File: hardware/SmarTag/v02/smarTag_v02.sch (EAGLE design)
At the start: 21 parts, among them U1 ADXL362

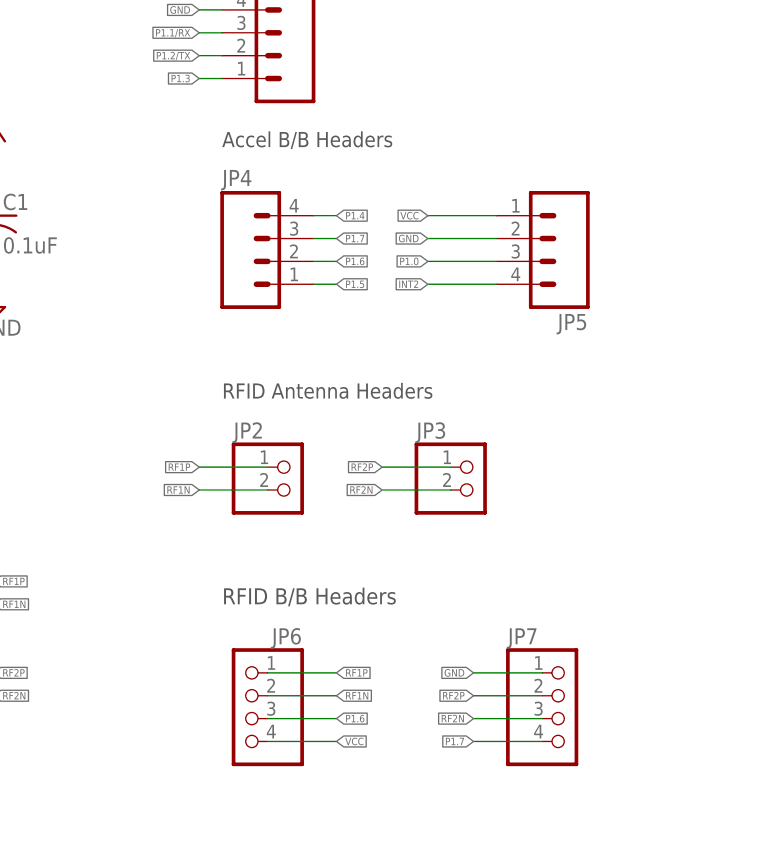
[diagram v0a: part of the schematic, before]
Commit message: hw: Remove JP4-7 from schematic. Add basic board.
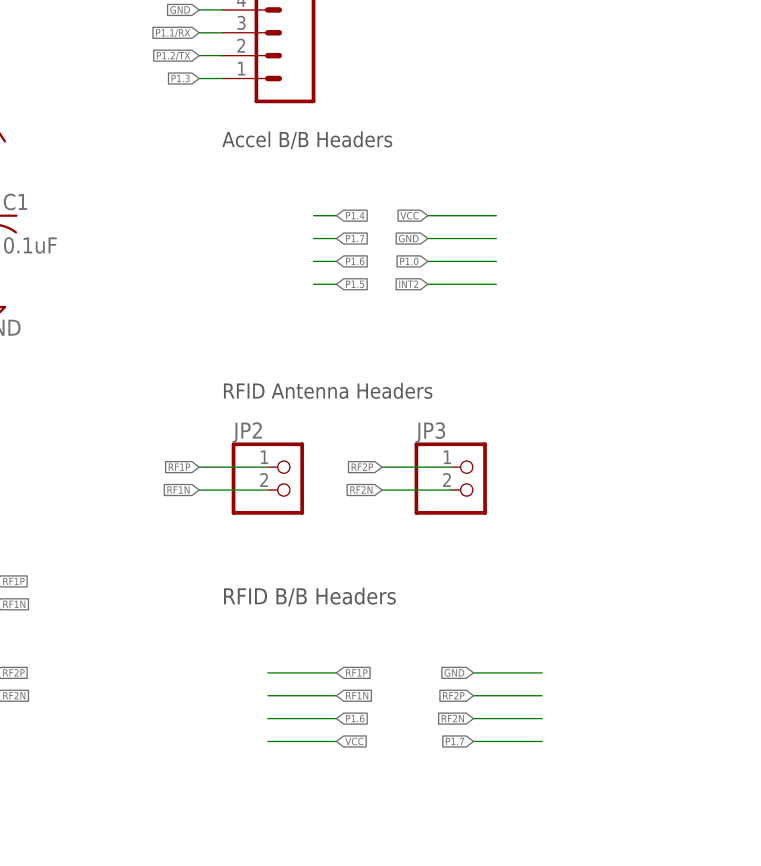
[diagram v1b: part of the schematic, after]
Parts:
- removed JP4, JP5: (no value), SparkFun-Connectors:M04LOCK
- removed JP6, JP7: (no value), pinhead:PINHD-1X4
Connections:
- net GND: no longer JP5.2, JP7.1
- net INT2: no longer JP5.4
- net P1.0: no longer JP5.3
- net P1.4: no longer JP4.4
- net P1.5: no longer JP4.1
- net P1.6: no longer JP4.2, JP6.3
- net P1.7: no longer JP4.3, JP7.4
- net RF1N: no longer JP6.2
- net RF1P: no longer JP6.1
- net RF2N: no longer JP7.3
- net RF2P: no longer JP7.2
- net VCC: no longer JP5.1, JP6.4
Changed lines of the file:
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@@
 <part name="P+4" library="supply1" deviceset="VCC" device=""/>
 <part name="SUPPLY1" library="supply2" deviceset="GND" device=""/>
-<part name="JP6" library="pinhead" deviceset="PINHD-1X4" device=""/>
-<part name="JP7" library="pinhead" deviceset="PINHD-1X4" device=""/>
 <part name="LED1" library="led" deviceset="LED" device="CHIP-LED0805"/>
 <part name="R3" library="rcl" deviceset="R-US_" device="R0805" value="470"/>
@@
 <part name="JP9" library="SparkFun-Connectors" deviceset="M05" device="LOCK"/>
 <part name="JP8" library="SparkFun-Connectors" deviceset="M03" device="LOCK"/>
-<part name="JP4" library="SparkFun-Connectors" deviceset="M04" device="LOCK"/>
 <part name="S1" library="switch-omron" deviceset="10-XX" device=""/>
-<part name="JP5" library="SparkFun-Connectors" deviceset="M04" device="LOCK"/>
 </parts>
 <sheets>
@@
 <instance part="P+4" gate="VCC" x="139.7" y="162.56" rot="R270"/>
 <instance part="SUPPLY1" gate="GND" x="119.38" y="160.02"/>
-<instance part="JP6" gate="A" x="119.38" y="30.48" rot="MR0"/>
-<instance part="JP7" gate="A" x="154.94" y="30.48"/>
 <instance part="LED1" gate="G$1" x="132.08" y="180.34" rot="R90"/>
 <instance part="R3" gate="G$1" x="119.38" y="180.34"/>
@@
 <instance part="JP9" gate="G$1" x="124.46" y="106.68" rot="MR0"/>
 <instance part="JP8" gate="G$1" x="160.02" y="134.62" rot="MR0"/>
-<instance part="JP4" gate="G$1" x="121.92" y="81.28"/>
 <instance part="S1" gate="1" x="162.56" y="180.34" rot="R270"/>
-<instance part="JP5" gate="G$1" x="152.4" y="83.82" rot="R180"/>
 </instances>
 <busses>
@@
 <wire x1="147.32" y1="86.36" x2="139.7" y2="86.36" width="0.1524" layer="91"/>
 <label x="139.7" y="86.36" size="0.8128" layer="91" rot="MR0" xref="yes"/>
-<pinref part="JP5" gate="G$1" pin="1"/>
 </segment>
 <segment>
@@
 </segment>
 <segment>
-<pinref part="JP6" gate="A" pin="4"/>
 <wire x1="121.92" y1="27.94" x2="129.54" y2="27.94" width="0.1524" layer="91"/>
 <label x="129.54" y="27.94" size="0.8128" layer="91" xref="yes"/>
@@
 <wire x1="147.32" y1="81.28" x2="139.7" y2="81.28" width="0.1524" layer="91"/>
 <label x="139.7" y="81.28" size="0.8128" layer="91" rot="MR0" xref="yes"/>
-<pinref part="JP5" gate="G$1" pin="3"/>
 </segment>
 </net>
@@
 <wire x1="127" y1="86.36" x2="129.54" y2="86.36" width="0.1524" layer="91"/>
 <label x="129.54" y="86.36" size="0.8128" layer="91" rot="MR180" xref="yes"/>
-<pinref part="JP4" gate="G$1" pin="4"/>
 </segment>
 </net>
@@
 <wire x1="129.54" y1="78.74" x2="127" y2="78.74" width="0.1524" layer="91"/>
 <label x="129.54" y="78.74" size="0.8128" layer="91" xref="yes"/>
-<pinref part="JP4" gate="G$1" pin="1"/>
 </segment>
 </net>
@@
 <wire x1="129.54" y1="83.82" x2="127" y2="83.82" width="0.1524" layer="91"/>
 <label x="129.54" y="83.82" size="0.8128" layer="91" rot="MR180" xref="yes"/>
-<pinref part="JP4" gate="G$1" pin="3"/>
-</segment>
-<segment>
-<pinref part="JP7" gate="A" pin="4"/>
+</segment>
+<segment>
 <wire x1="152.4" y1="27.94" x2="144.78" y2="27.94" width="0.1524" layer="91"/>
 <label x="144.78" y="27.94" size="0.8128" layer="91" rot="MR0" xref="yes"/>
@@
 <wire x1="127" y1="81.28" x2="129.54" y2="81.28" width="0.1524" layer="91"/>
 <label x="129.54" y="81.28" size="0.8128" layer="91" rot="MR180" xref="yes"/>
-<pinref part="JP4" gate="G$1" pin="2"/>
-</segment>
-<segment>
-<pinref part="JP6" gate="A" pin="3"/>
+</segment>
+<segment>
 <wire x1="121.92" y1="30.48" x2="129.54" y2="30.48" width="0.1524" layer="91"/>
 <label x="129.54" y="30.48" size="0.8128" layer="91" xref="yes"/>
@@
 <wire x1="139.7" y1="83.82" x2="147.32" y2="83.82" width="0.1524" layer="91"/>
 <label x="139.7" y="83.82" size="0.8128" layer="91" rot="MR0" xref="yes"/>
-<pinref part="JP5" gate="G$1" pin="2"/>
 </segment>
 <segment>
@@
 </segment>
 <segment>
-<pinref part="JP7" gate="A" pin="1"/>
 <wire x1="152.4" y1="35.56" x2="144.78" y2="35.56" width="0.1524" layer="91"/>
 <label x="144.78" y="35.56" size="0.8128" layer="91" rot="MR0" xref="yes"/>
@@
 </segment>
 <segment>
-<pinref part="JP6" gate="A" pin="1"/>
 <wire x1="121.92" y1="35.56" x2="129.54" y2="35.56" width="0.1524" layer="91"/>
 <label x="129.54" y="35.56" size="0.8128" layer="91" xref="yes"/>
@@
 </segment>
 <segment>
-<pinref part="JP6" gate="A" pin="2"/>
 <wire x1="129.54" y1="33.02" x2="121.92" y2="33.02" width="0.1524" layer="91"/>
 <label x="129.54" y="33.02" size="0.8128" layer="91" xref="yes"/>
@@
 </segment>
 <segment>
-<pinref part="JP7" gate="A" pin="3"/>
 <wire x1="152.4" y1="30.48" x2="144.78" y2="30.48" width="0.1524" layer="91"/>
 <label x="144.78" y="30.48" size="0.8128" layer="91" rot="MR0" xref="yes"/>
@@
 </segment>
 <segment>
-<pinref part="JP7" gate="A" pin="2"/>
 <wire x1="152.4" y1="33.02" x2="144.78" y2="33.02" width="0.1524" layer="91"/>
 <label x="144.78" y="33.02" size="0.8128" layer="91" rot="MR0" xref="yes"/>
@@
 <wire x1="139.7" y1="78.74" x2="147.32" y2="78.74" width="0.1524" layer="91"/>
 <label x="139.7" y="78.74" size="0.8128" layer="91" rot="MR0" xref="yes"/>
-<pinref part="JP5" gate="G$1" pin="4"/>
-</segment>
-<segment>
+</segment>
+<segment>

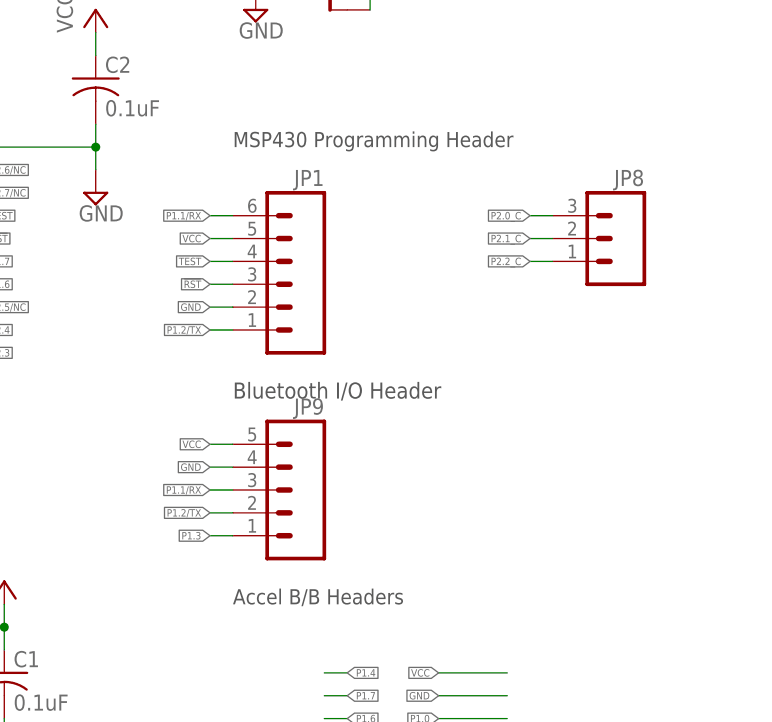
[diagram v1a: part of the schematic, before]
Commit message: hw: Renumber JP headers and fix BT header.
Remove P1.3 signal from BT daughter board header.
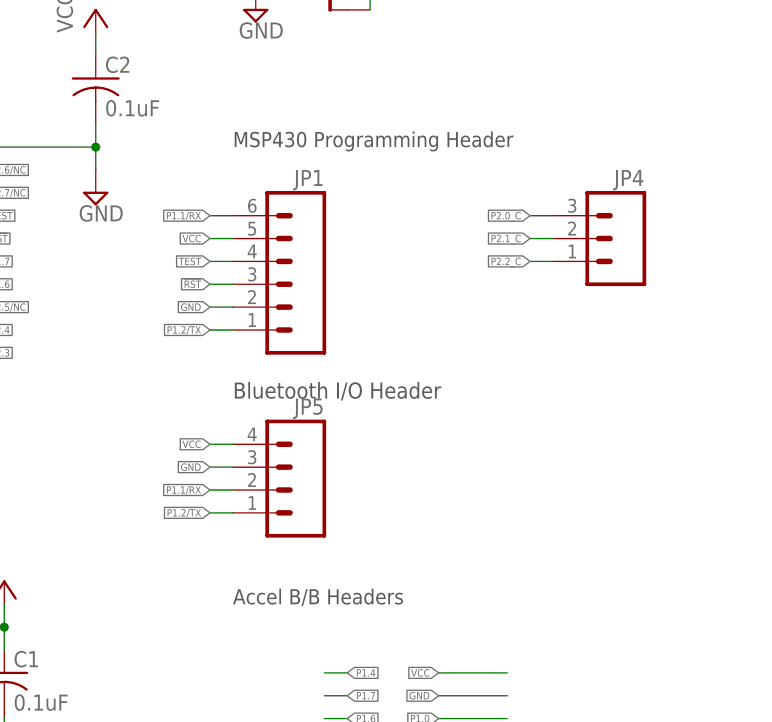
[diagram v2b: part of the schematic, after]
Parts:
- removed JP9: (no value), SparkFun-Connectors:M05LOCK
- added JP5: (no value), SparkFun-Connectors:M04LOCK
- renumbered JP8 to JP4
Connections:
- net GND: now also JP5.3; no longer JP9.4
- net P1.1/RX: now also JP5.2; no longer JP9.3
- net P1.2/TX: now also JP5.1; no longer JP9.2
- net P1.3: no longer JP9.1
- net VCC: now also JP5.4; no longer JP9.5
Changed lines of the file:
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@@
 <part name="SUPPLY5" library="supply2" deviceset="GND" device=""/>
 <part name="JP1" library="SparkFun-Connectors" deviceset="M06" device="LOCK"/>
-<part name="JP9" library="SparkFun-Connectors" deviceset="M05" device="LOCK"/>
-<part name="JP8" library="SparkFun-Connectors" deviceset="M03" device="LOCK"/>
+<part name="JP4" library="SparkFun-Connectors" deviceset="M03" device="LOCK"/>
 <part name="S1" library="switch-omron" deviceset="10-XX" device=""/>
+<part name="JP5" library="SparkFun-Connectors" deviceset="M04" device="LOCK"/>
 </parts>
 <sheets>
@@
 <instance part="SUPPLY5" gate="GND" x="142.24" y="177.8"/>
 <instance part="JP1" gate="G$1" x="121.92" y="129.54" rot="MR0"/>
-<instance part="JP9" gate="G$1" x="124.46" y="106.68" rot="MR0"/>
-<instance part="JP8" gate="G$1" x="160.02" y="134.62" rot="MR0"/>
+<instance part="JP4" gate="G$1" x="160.02" y="134.62" rot="MR0"/>
 <instance part="S1" gate="1" x="162.56" y="180.34" rot="R270"/>
+<instance part="JP5" gate="G$1" x="121.92" y="106.68" rot="MR0"/>
 </instances>
 <busses>
@@
 <wire x1="116.84" y1="111.76" x2="114.3" y2="111.76" width="0.1524" layer="91"/>
 <label x="114.3" y="111.76" size="0.8128" layer="91" rot="MR0" xref="yes"/>
-<pinref part="JP9" gate="G$1" pin="5"/>
+<pinref part="JP5" gate="G$1" pin="4"/>
 </segment>
 </net>
@@
 <wire x1="116.84" y1="106.68" x2="114.3" y2="106.68" width="0.1524" layer="91"/>
 <label x="114.3" y="106.68" size="0.8128" layer="91" rot="MR0" xref="yes"/>
-<pinref part="JP9" gate="G$1" pin="3"/>
+<pinref part="JP5" gate="G$1" pin="2"/>
 </segment>
 </net>
@@
 <wire x1="116.84" y1="104.14" x2="114.3" y2="104.14" width="0.1524" layer="91"/>
 <label x="114.3" y="104.14" size="0.8128" layer="91" rot="MR0" xref="yes"/>
-<pinref part="JP9" gate="G$1" pin="2"/>
+<pinref part="JP5" gate="G$1" pin="1"/>
 </segment>
 </net>
@@
 <wire x1="152.4" y1="137.16" x2="149.86" y2="137.16" width="0.1524" layer="91"/>
 <label x="149.86" y="137.16" size="0.8128" layer="91" rot="MR0" xref="yes"/>
-<pinref part="JP8" gate="G$1" pin="3"/>
+<pinref part="JP4" gate="G$1" pin="3"/>
 </segment>
 </net>
@@
 <wire x1="152.4" y1="134.62" x2="149.86" y2="134.62" width="0.1524" layer="91"/>
 <label x="149.86" y="134.62" size="0.8128" layer="91" rot="MR0" xref="yes"/>
-<pinref part="JP8" gate="G$1" pin="2"/>
+<pinref part="JP4" gate="G$1" pin="2"/>
 </segment>
 </net>
@@
 <wire x1="152.4" y1="132.08" x2="149.86" y2="132.08" width="0.1524" layer="91"/>
 <label x="149.86" y="132.08" size="0.8128" layer="91" rot="MR0" xref="yes"/>
-<pinref part="JP8" gate="G$1" pin="1"/>
+<pinref part="JP4" gate="G$1" pin="1"/>
 </segment>
 </net>
@@
 <wire x1="116.84" y1="109.22" x2="114.3" y2="109.22" width="0.1524" layer="91"/>
 <label x="114.3" y="109.22" size="0.8128" layer="91" rot="MR0" xref="yes"/>
-<pinref part="JP9" gate="G$1" pin="4"/>
+<pinref part="JP5" gate="G$1" pin="3"/>
 </segment>
 <segment>
@@
 <net name="P1.3" class="0">
 <segment>
-<wire x1="116.84" y1="101.6" x2="114.3" y2="101.6" width="0.1524" layer="91"/>
-<label x="114.3" y="101.6" size="0.8128" layer="91" rot="MR0" xref="yes"/>
-<pinref part="JP9" gate="G$1" pin="1"/>
-</segment>
-<segment>
 <pinref part="MCU1" gate="G$1" pin="5"/>
